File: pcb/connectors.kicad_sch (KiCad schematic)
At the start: 3 parts, among them J1 GPIO, J2 Hirose_FH12-16S, J3 TC2030

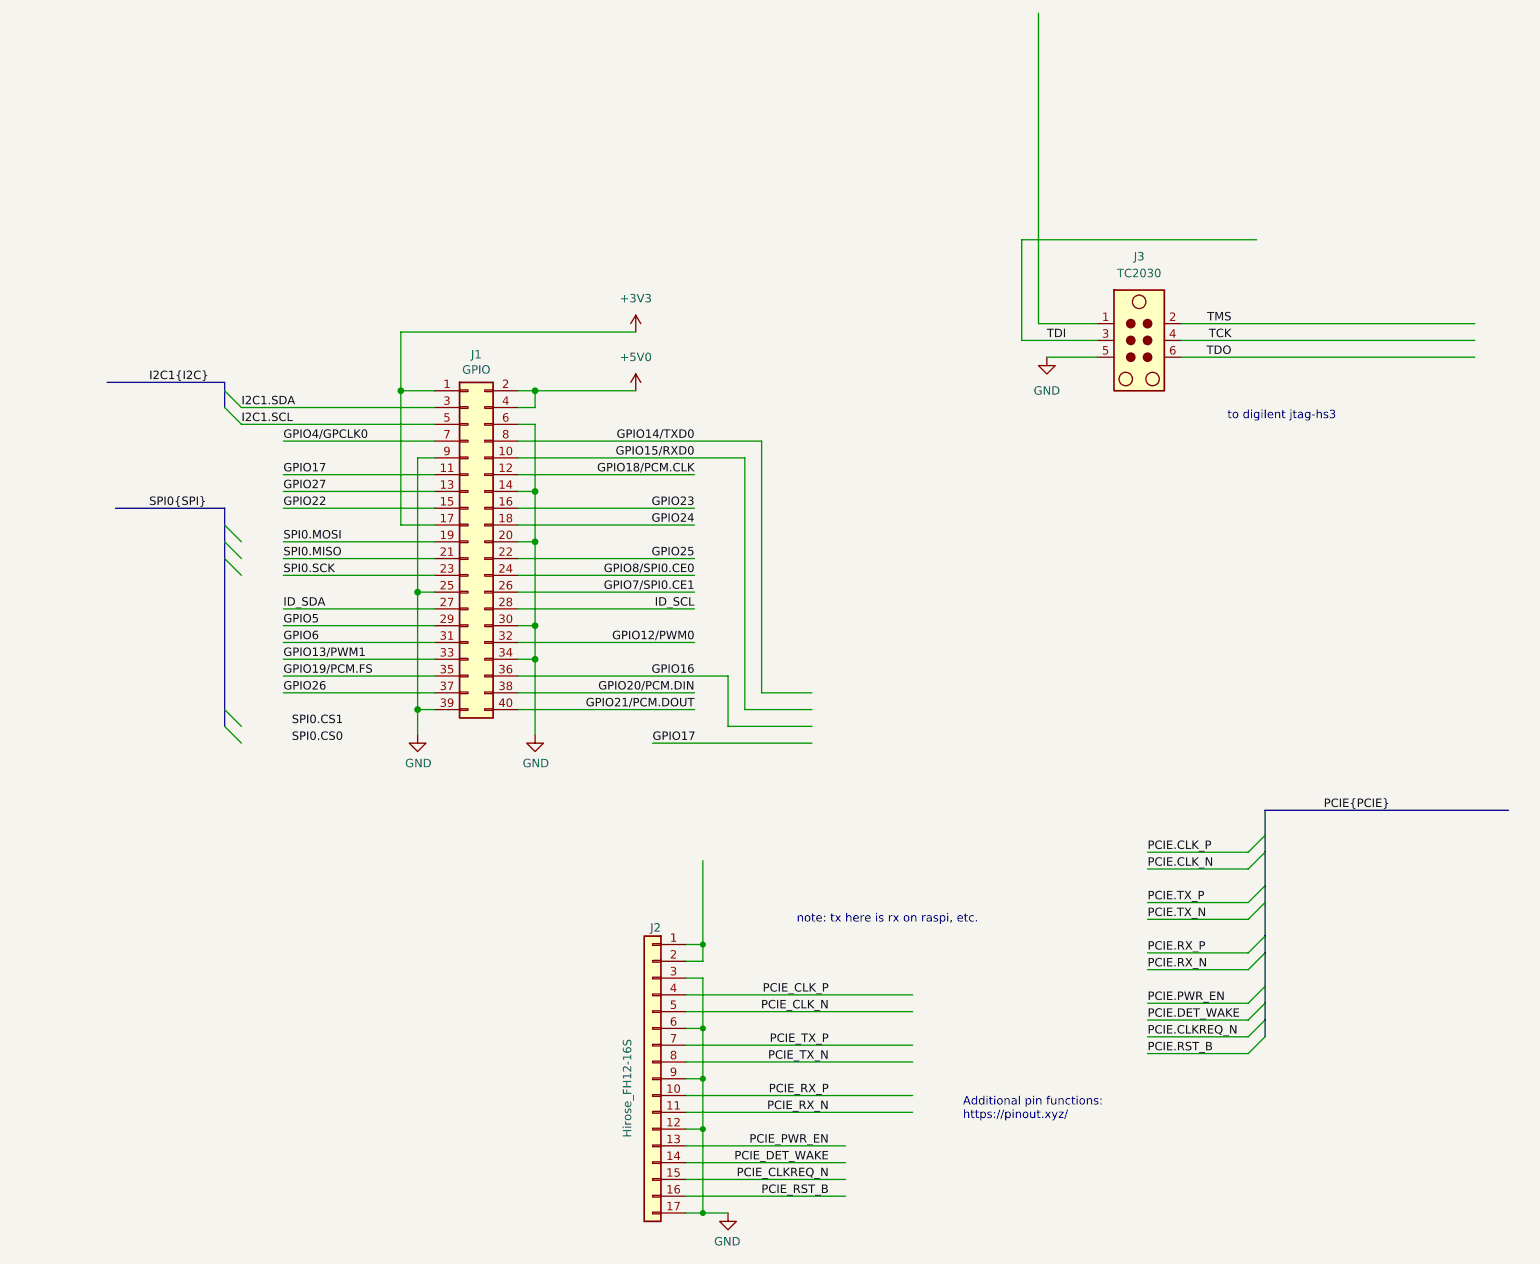
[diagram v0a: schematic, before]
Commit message: completed bus aliasing definitions
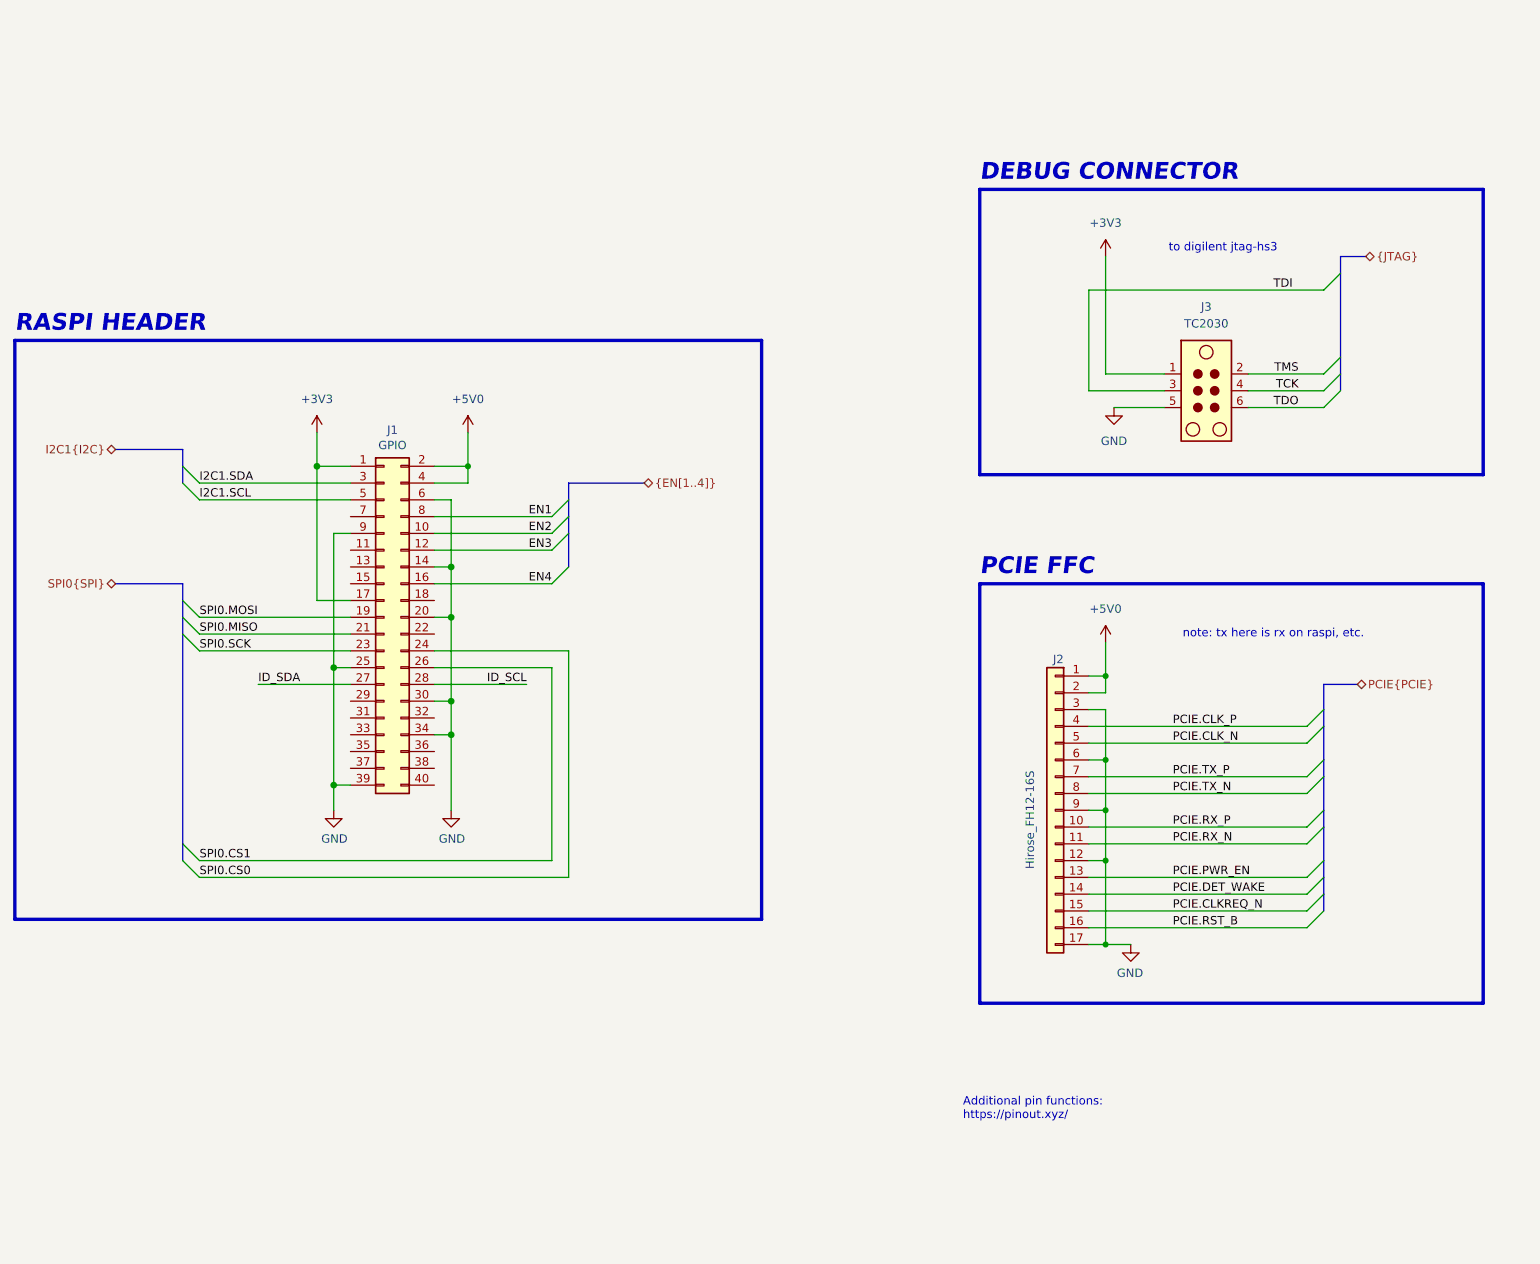
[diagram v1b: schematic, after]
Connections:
- net GPIO7/SPI0.CE1 is gone; now on net SPI0.CS1: J1.26 (Pin_26)
- net GPIO8/SPI0.CE0 is gone; now on net SPI0.CS0: J1.24 (Pin_24)
- net PCIE_CLKREQ_N is gone; now on net PCIE.CLKREQ_N: J2.15 (Pin_15)
- net PCIE_CLK_N is gone; now on net PCIE.CLK_N: J2.5 (Pin_5)
- net PCIE_CLK_P is gone; now on net PCIE.CLK_P: J2.4 (Pin_4)
- net PCIE_DET_WAKE is gone; now on net PCIE.DET_WAKE: J2.14 (Pin_14)
- net PCIE_PWR_EN is gone; now on net PCIE.PWR_EN: J2.13 (Pin_13)
- net PCIE_RST_B is gone; now on net PCIE.RST_B: J2.16 (Pin_16)
- net PCIE_RX_N is gone; now on net PCIE.RX_N: J2.11 (Pin_11)
- net PCIE_RX_P is gone; now on net PCIE.RX_P: J2.10 (Pin_10)
- net PCIE_TX_N is gone; now on net PCIE.TX_N: J2.8 (Pin_8)
- net PCIE_TX_P is gone; now on net PCIE.TX_P: J2.7 (Pin_7)
- net +3V3: now also J3.1
- net +5V0: now also J2.1 (Pin_1), J2.2 (Pin_2)
- net GPIO12/PWM0: no longer names the net of J1.32 (Pin_32)
- net GPIO13/PWM1: no longer names the net of J1.33 (Pin_33)
- net GPIO14/TXD0 renamed EN1
- net GPIO15/RXD0 renamed EN2
- net GPIO16: no longer names the net of J1.36 (Pin_36)
- net GPIO17: no longer names the net of J1.11 (Pin_11)
- net GPIO18/PCM.CLK renamed EN3
- net GPIO19/PCM.FS: no longer names the net of J1.35 (Pin_35)
- net GPIO20/PCM.DIN: no longer names the net of J1.38 (Pin_38)
- net GPIO21/PCM.DOUT: no longer names the net of J1.40 (Pin_40)
- net GPIO22: no longer names the net of J1.15 (Pin_15)
- net GPIO23 renamed EN4
- net GPIO24: no longer names the net of J1.18 (Pin_18)
- net GPIO25: no longer names the net of J1.22 (Pin_22)
- net GPIO26: no longer names the net of J1.37 (Pin_37)
- net GPIO27: no longer names the net of J1.13 (Pin_13)
- net GPIO4/GPCLK0: no longer names the net of J1.7 (Pin_7)
- net GPIO5: no longer names the net of J1.29 (Pin_29)
- net GPIO6: no longer names the net of J1.31 (Pin_31)
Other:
- note added: "DEBUG CONNECTOR"
- note added: "PCIE FFC"
- note added: "RASPI HEADER"
- moved on the sheet: J1, J2, J3

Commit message: updated sims, power hierarchy
added power flags to voltage buses, removed standard kicad "+3.3V" power flags and using standard kicad "power flag" in order to use hierarchical labels to visually show power paths
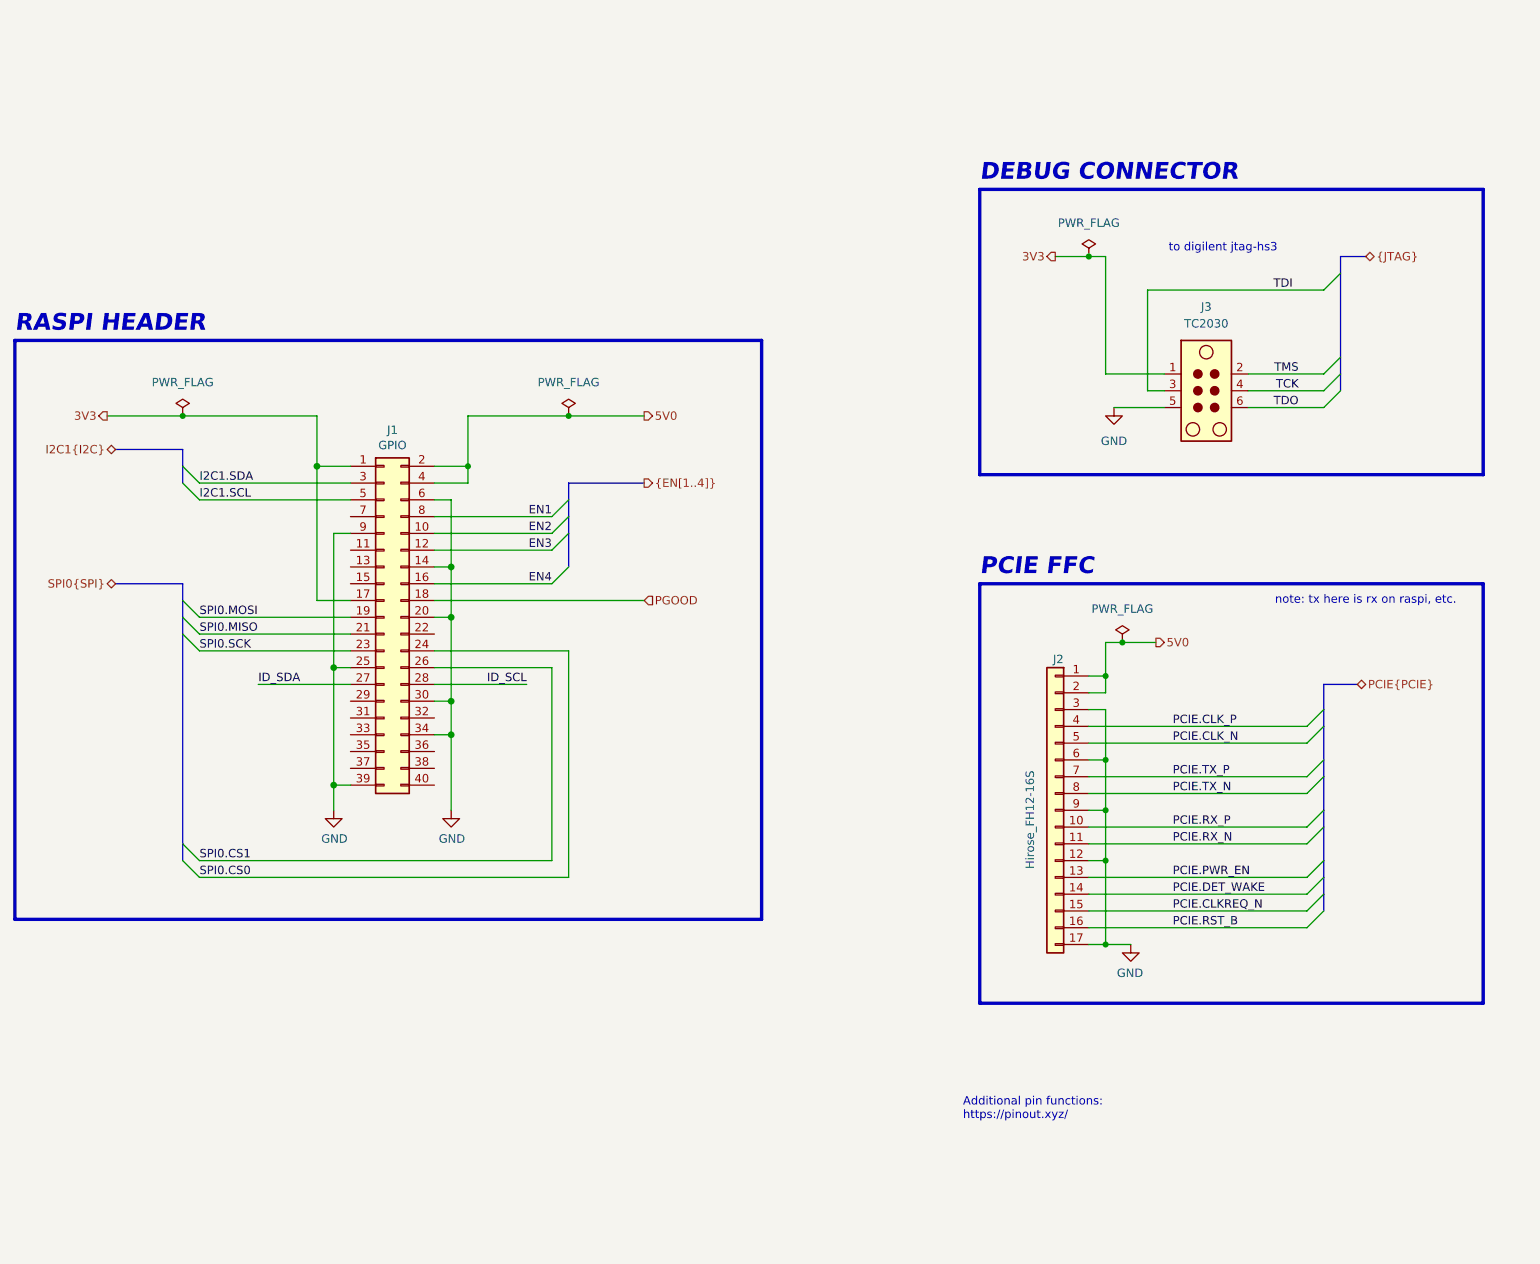
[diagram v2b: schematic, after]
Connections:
- net PGOOD: now reaches J1.18 (Pin_18)
- net +3V3 renamed 3V3
- net +5V0 renamed 5V0

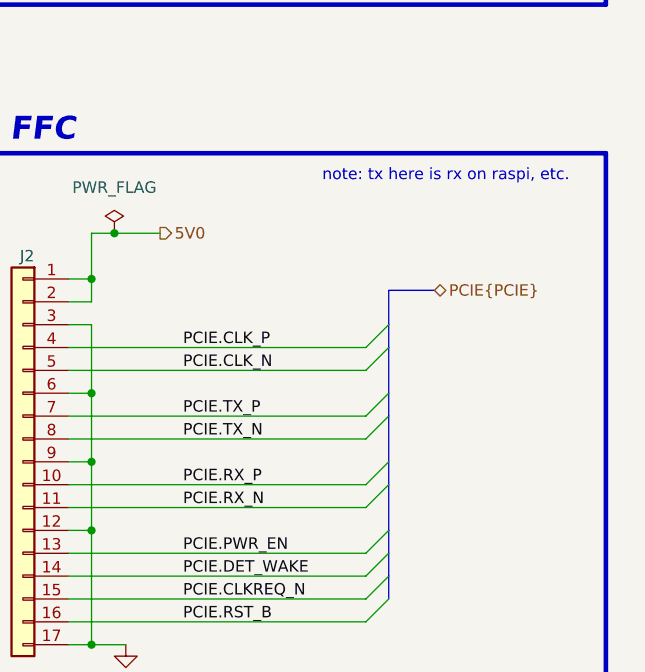
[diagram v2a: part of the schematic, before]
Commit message: hierarchical current sense
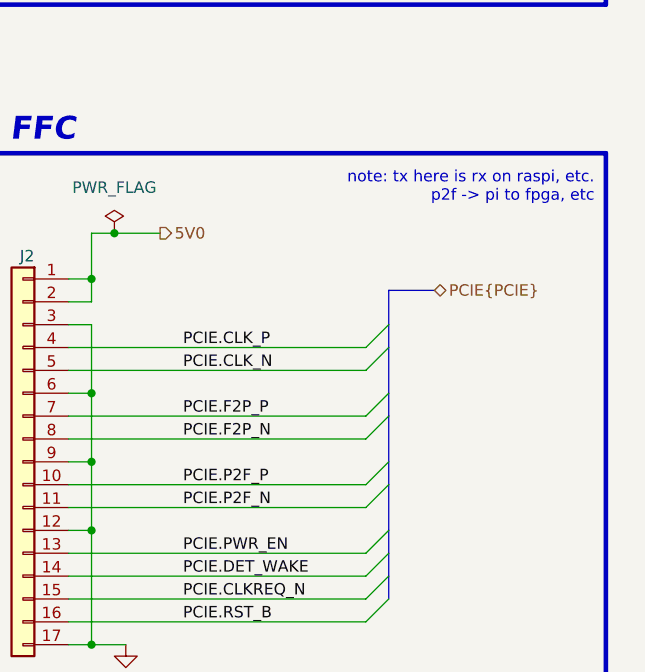
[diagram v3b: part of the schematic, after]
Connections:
- net PCIE.RX_N renamed PCIE.P2F_N
- net PCIE.RX_P renamed PCIE.P2F_P
- net PCIE.TX_N renamed PCIE.F2P_N
- net PCIE.TX_P renamed PCIE.F2P_P
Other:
- note added: "note: tx here is rx on raspi, etc. p2f -> pi to fpga, etc"
- note removed: "note: tx here is rx on raspi, etc."
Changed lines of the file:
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@@
 	)
 	(bus_alias "PCIE"
-		(members "CLK_P" "CLK_N" "TX_P" "TX_N" "RX_P" "RX_N" "PWR_EN" "DET_WAKE"
+		(members "CLK_P" "CLK_N" "F2P_P" "F2P_N" "P2F_P" "P2F_N" "PWR_EN" "DET_WAKE"
 			"CLKREQ_N" "RST_B"
 		)
@@
 		)
 	)
-	(text "note: tx here is rx on raspi, etc."
+	(text "note: tx here is rx on raspi, etc.\np2f -> pi to fpga, etc"
 		(exclude_from_sim no)
-		(at 238.76 92.71 0)
-		(effects
-			(font
-				(size 1.27 1.27)
-			)
+		(at 255.27 93.98 0)
+		(effects
+			(font
+				(size 1.27 1.27)
+			)
+			(justify right)
 		)
 	)
@@
 		)
 	)
-	(label "PCIE.TX_P"
+	(label "PCIE.F2P_P"
 		(at 209.55 119.38 0)
 		(effects
@@
 		)
 	)
-	(label "PCIE.RX_N"
+	(label "PCIE.P2F_N"
 		(at 209.55 129.54 0)
 		(effects
@@
 		)
 	)
-	(label "PCIE.RX_P"
+	(label "PCIE.P2F_P"
 		(at 209.55 127 0)
 		(effects
@@
 		)
 	)
-	(label "PCIE.TX_N"
+	(label "PCIE.F2P_N"
 		(at 209.55 121.92 0)
 		(effects

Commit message: pcie definitions
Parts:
- added R?: 2.2K, Resistor_SMD:R_0402_1005Metric, symbol Device:R_US
- added R?: 100K, Resistor_SMD:R_0402_1005Metric, symbol Device:R_US
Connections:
- net 3V3: now also R?.1
- net GND: now also R?.2
- net PCIE.DET_WAKE: now also R?.2
- net PCIE.PWR_EN: now also R?.1

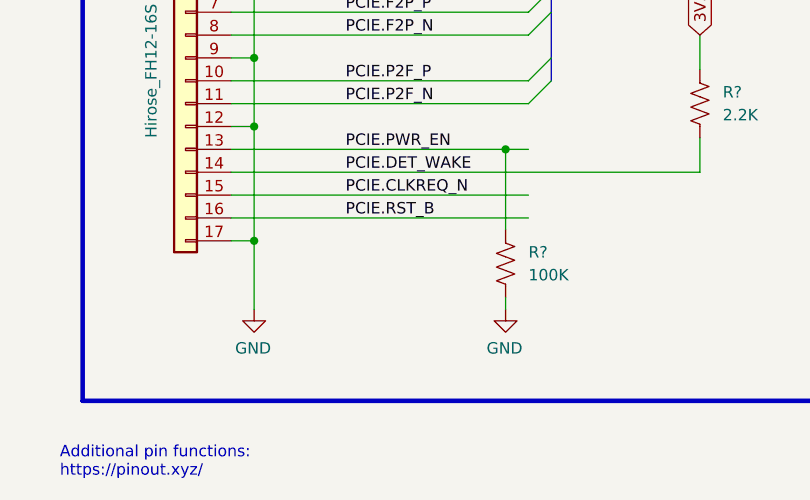
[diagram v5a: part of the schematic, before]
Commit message: decoupling for 3v3_fd
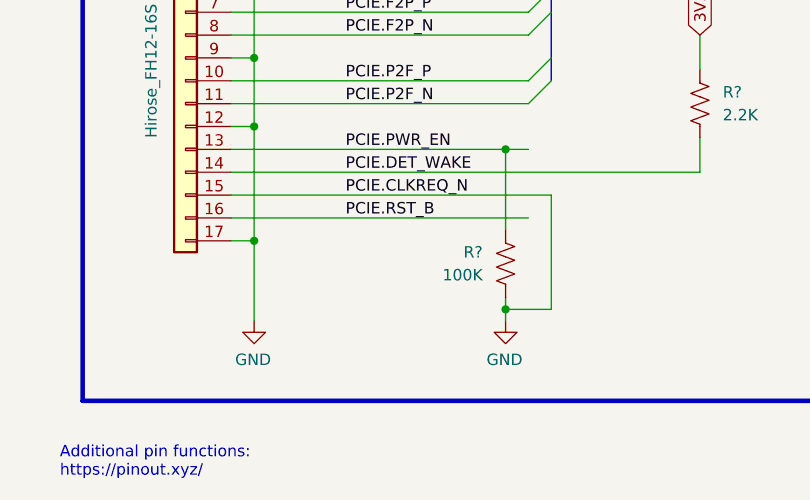
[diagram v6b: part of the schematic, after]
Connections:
- net PCIE.CLKREQ_N is gone; now on net GND: J2.15 (Pin_15)
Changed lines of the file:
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@@
+	)
+	(junction
+		(at 227.33 152.4)
+		(diameter 0)
+		(color 0 0 0 0)
 	)
 	(junction
@@
 	(wire
 		(pts
+			(xy 227.33 152.4) (xy 227.33 151.13)
+		)
+		(stroke
+			(width 0)
+			(type default)
+		)
+	)
+	(wire
+		(pts
 			(xy 199.39 124.46) (xy 196.85 124.46)
 		)
@@
 	(wire
 		(pts
+			(xy 227.33 152.4) (xy 227.33 153.67)
+		)
+		(stroke
+			(width 0)
+			(type default)
+		)
+	)
+	(wire
+		(pts
 			(xy 100.33 113.03) (xy 97.79 113.03)
 		)
@@
 	(wire
 		(pts
+			(xy 232.41 152.4) (xy 227.33 152.4)
+		)
+		(stroke
+			(width 0)
+			(type default)
+		)
+	)
+	(wire
+		(pts
 			(xy 196.85 114.3) (xy 229.87 114.3)
 		)
@@
 	(wire
 		(pts
-			(xy 196.85 139.7) (xy 229.87 139.7)
+			(xy 196.85 139.7) (xy 232.41 139.7)
 		)
 		(stroke
@@
 	(wire
 		(pts
-			(xy 199.39 144.78) (xy 199.39 152.4)
+			(xy 199.39 144.78) (xy 199.39 153.67)
 		)
 		(stroke
@@
 	(wire
 		(pts
+			(xy 232.41 139.7) (xy 232.41 152.4)
+		)
+		(stroke
+			(width 0)
+			(type default)
+		)
+	)
+	(wire
+		(pts
 			(xy 82.55 82.55) (xy 85.09 82.55)
 		)
@@
 			(width 0)
 			(type solid)
-		)
-	)
-	(wire
-		(pts
-			(xy 227.33 151.13) (xy 227.33 152.4)
-		)
-		(stroke
-			(width 0)
-			(type default)
 		)
 	)
@@
 	(symbol
 		(lib_id "power:GND")
-		(at 199.39 152.4 0)
+		(at 199.39 153.67 0)
 		(mirror y)
 		(unit 1)
@@
 		(dnp no)
 		(property "Reference" "#PWR08"
-			(at 199.39 158.75 0)
+			(at 199.39 160.02 0)
 			(effects
 				(font
@@
 		)
 		(property "Value" "GND"
-			(at 199.2757 156.7244 0)
+			(at 199.2757 157.9944 0)
 			(effects
 				(font
@@
 		)
 		(property "Footprint" ""
-			(at 199.39 152.4 0)
+			(at 199.39 153.67 0)
 			(effects
 				(font
@@
 		)
 		(property "Datasheet" ""
-			(at 199.39 152.4 0)
+			(at 199.39 153.67 0)
 			(effects
 				(font
@@
 		)
 		(property "Description" "Power symbol creates a global label with name \"GND\" , ground"
-			(at 199.39 152.4 0)
+			(at 199.39 153.67 0)
 			(effects
 				(font
@@
 		(on_board yes)
 		(dnp no)
-		(fields_autoplaced yes)
 		(property "Reference" "R?"
-			(at 229.87 146.0499 0)
-			(effects
-				(font
-					(size 1.27 1.27)
-				)
-				(justify left)
+			(at 224.79 146.05 0)
+			(effects
+				(font
+					(size 1.27 1.27)
+				)
+				(justify right)
 			)
 		)
 		(property "Value" "100K"
-			(at 229.87 148.5899 0)
-			(effects
-				(font
-					(size 1.27 1.27)
-				)
-				(justify left)
+			(at 224.79 148.59 0)
+			(effects
+				(font
+					(size 1.27 1.27)
+				)
+				(justify right)
 			)
 		)
@@
 	(symbol
 		(lib_id "power:GND")
-		(at 227.33 152.4 0)
+		(at 227.33 153.67 0)
 		(mirror y)
 		(unit 1)
@@
 		(dnp no)
 		(property "Reference" "#PWR030"
-			(at 227.33 158.75 0)
+			(at 227.33 160.02 0)
 			(effects
 				(font
@@
 		)
 		(property "Value" "GND"
-			(at 227.2157 156.7244 0)
+			(at 227.2157 157.9944 0)
 			(effects
 				(font
@@
 		)
 		(property "Footprint" ""
-			(at 227.33 152.4 0)
+			(at 227.33 153.67 0)
 			(effects
 				(font
@@
 		)
 		(property "Datasheet" ""
-			(at 227.33 152.4 0)
+			(at 227.33 153.67 0)
 			(effects
 				(font
@@
 		)
 		(property "Description" "Power symbol creates a global label with name \"GND\" , ground"
-			(at 227.33 152.4 0)
-			(effects
-				(font
+			(at 227.33 153.67 0)
+			(effects
+				(font
